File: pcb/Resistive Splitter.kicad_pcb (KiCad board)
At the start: 2 copper layers, 75 x 40 mm, 6 parts, among them J1 SMA 50, J2 SMA 50, J3 SMA 50

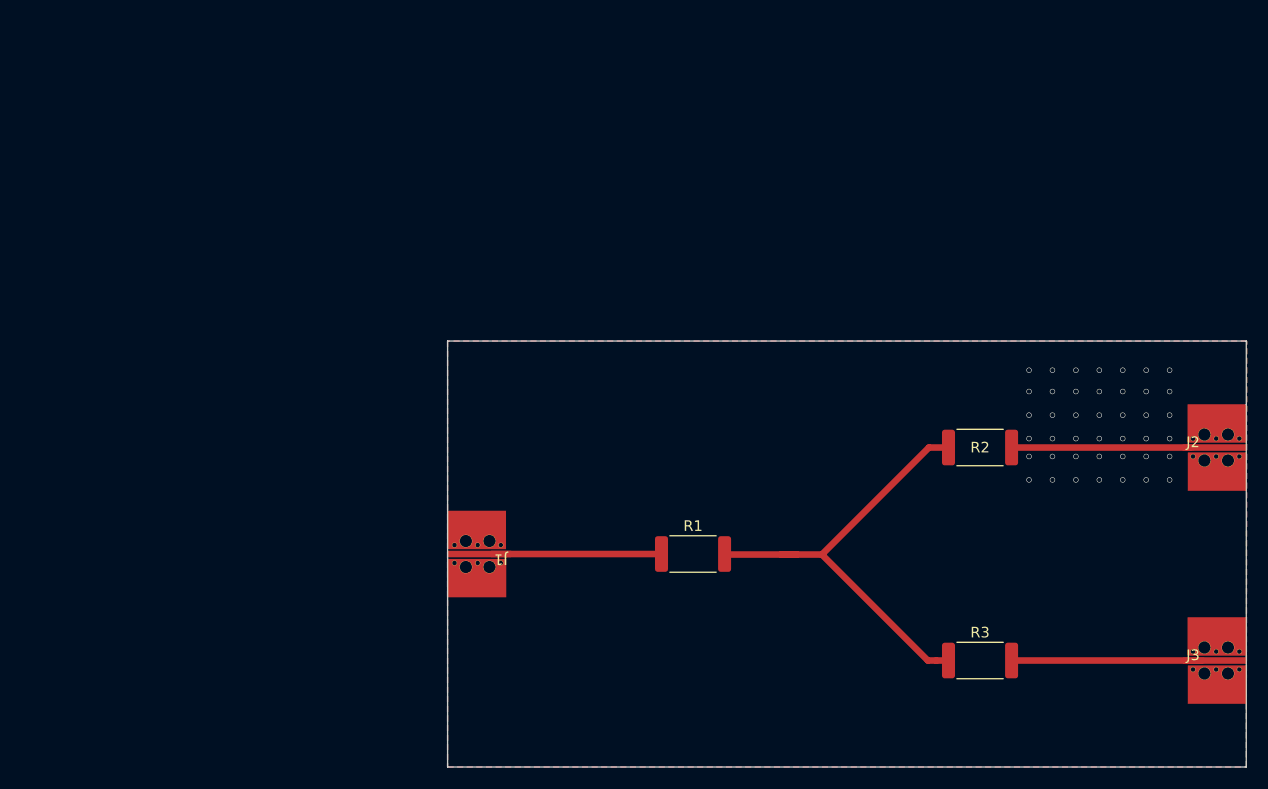
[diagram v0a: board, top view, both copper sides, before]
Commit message: Simulation Beginnings
Simmulation traces and and plotting S21 and S11
have sub repo setup with openems
have venv setup
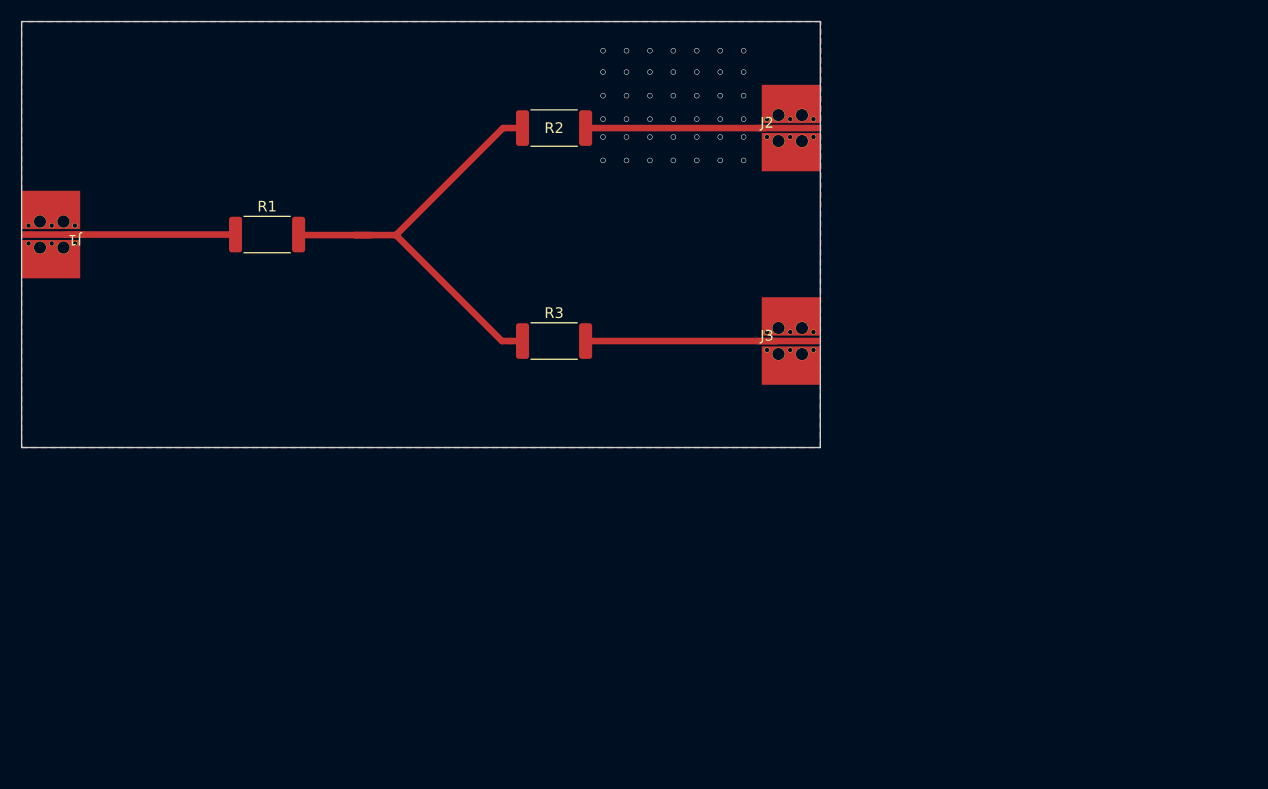
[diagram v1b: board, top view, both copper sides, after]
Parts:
- moved J1 50.0 mm to (5.00, 20.0)
- moved J2 50.0 mm to (70.0, 10.0)
- moved J3 50.0 mm to (70.0, 30.0)
- moved R1 50.0 mm to (23.1, 20.0)
- moved R2 50.0 mm to (50.0, 10.0)
- moved R3 50.0 mm to (50.0, 30.0)
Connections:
- J1 pad 2: (no net) -> GND
- J3 pad 2: (no net) -> GND
